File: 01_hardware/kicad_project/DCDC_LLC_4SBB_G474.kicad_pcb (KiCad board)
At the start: 4 copper layers, 160 x 105 mm, 237 parts, among them J1 VIN, J2 VOUT, J3 CAN, J4 CAN, J5 ADDR, J6 PROG, J7 SWD, Q1 NCEP0140AG, Q2 NCEP0160AG, Q3 NCEP0160AG, Q4 NCEP0140AG, Q5 NCEP0160AG, Q6 NCEP0160AG, Q7 BSC160N15NS5, Q8 BSC160N15NS5, SW1 DIP-6, T1 PQ2620, U1 STM32G474RBT6, U10 UCC27211DDAR, U11 UCC27524DR, U12 CA-IS3642LVW, U13 LMR16006XDDCR, U14 AMS1117-5.0, U15 LMV331IDBVR, U16 TL431AIDBZR, U2 UCC27211DDAR, U3 UCC27211DDAR, U4 LMR16006XDDCR, U5 AMS1117-5.0, U7 INA181A1IDBVR, U8 INA181A2IDBVR, U9 CA-IS3062VW, Y1 16MHz

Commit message: VIN monitor: sawtooth/comparator PWM over spare isolator channel to PA2 (TIM15_CH1)
- Primary: PNP current-source ramp (~5 ms) into 47 nF C0G, U17 reset detector,
  U18 PWM comparator vs OVP_DIV; R81/R82 now 0.1 %
- U12 VI2->VO2 carries VIN_PWM to PA2; R93 is its pull-down
- PCB: new block placed/routed below U15/U16, R106 moved for courtyard,
  GNDP island vias, silkscreen for new parts; DRC clean, netlist parity OK
- Outputs regenerated (BOM, Gerbers, CPL, EasyEDA, PDFs, pin-map)

Co-Authored-By: Claude Opus 5.5 <noreply@anthropic.com>
Claude-Session: https://claude.ai/code/session_01A35wrnwFKLPSaRSxxHs471
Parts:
- added C81: 1n, C_0402_1005Metric, F.Cu at (49.0, 96.0)
- added C82: 47n C0G 50V, C_0805_2012Metric, F.Cu at (47.4, 89.0)
- added C83: 100n, C_0402_1005Metric, F.Cu at (52.0, 86.4)
- added C84: 100n, C_0402_1005Metric, F.Cu at (60.0, 86.4)
- added D7: 1N4148W, D_SOD-123, F.Cu at (52.0, 93.6)
- added Q10: 2N7002, SOT-23, F.Cu at (46.6, 95.4)
- added Q9: MMBT3906, SOT-23, F.Cu at (43.4, 89.0)
- added R106: 1k, R_0402_1005Metric, F.Cu at (56.1, 92.0)
- added R107: 22k, R_0402_1005Metric, F.Cu at (50.4, 96.0)
- added R108: 10k, R_0402_1005Metric, F.Cu at (63.1, 88.6)
- added R109: 10k, R_0402_1005Metric, F.Cu at (56.9, 89.0)
- added R110: 1M, R_0402_1005Metric, F.Cu at (60.0, 91.6)
- added R86: 56k 1%, R_0402_1005Metric, F.Cu at (43.4, 85.8)
- added R87: 10k 1%, R_0402_1005Metric, F.Cu at (40.2, 87.6)
- added R88: 15k 1%, R_0402_1005Metric, F.Cu at (40.2, 90.6)
- added R89: 22R, R_0402_1005Metric, F.Cu at (46.6, 92.2)
- added U17: LMV331IDBVR, SOT-23-5, F.Cu at (52.0, 89.0)
- added U18: LMV331IDBVR, SOT-23-5, F.Cu at (60.0, 89.0)
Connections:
- R93 pad 1: SP_PA2 -> VIN_PWM
- U1 pad 14: SP_PA2 -> VIN_PWM
- U12 pad 13: (no net) -> VIN_PWM
- U12 pad 4: GNDP -> VINPWM_P
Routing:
- net VIN_PWM: track 0.00 -> 54.4 mm, vias 0 -> 4
- net +5V_P: track 68.5 -> 105.7 mm
- net VINPWM_P: track 0.00 -> 27.2 mm
- net RAMP_P: track 0.00 -> 17.7 mm, vias 0 -> 2
- net GATE_P: track 0.00 -> 13.9 mm
- net OVP_DIV: track 22.3 -> 33.7 mm, vias 2 -> 4
- net PB_P: track 0.00 -> 10.7 mm
- net VREF_P: track 10.1 -> 19.6 mm, vias 2 -> 4
- net RST_P: track 0.00 -> 8.25 mm
- net RAMPS_P: track 0.00 -> 7.21 mm
- net PE_P: track 0.00 -> 4.95 mm, vias 0 -> 2
- net SP_PA2: track 3.14 -> 0.00 mm
- net DIS_P: track 0.00 -> 2.85 mm
- net SR2_PWM: track 61.3 -> 58.8 mm
- net GNDP: track 105.4 -> 103.5 mm, vias 252 -> 245
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
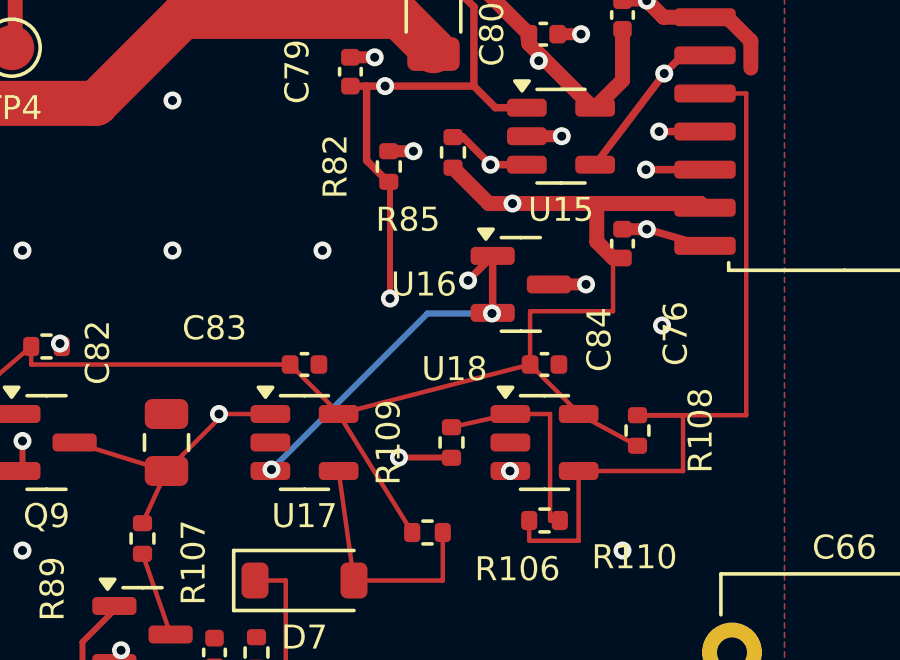
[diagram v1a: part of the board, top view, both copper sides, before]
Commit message: Review fixes: VIN monitor linearity and reset, full-scale summary, design notes
- U18 inputs swapped (IN+ = OVP_DIV, IN- = RAMP via R109 1k); R110 4.7M
  hysteresis now on the divider, not the ramp (old 1M path bent the ramp:
  +12.5 % error at 12 V; now < 0.02 % in simulation)
- Reset pulse hardened: C81 220p C0G, R107 100k so C82 always fully discharges
- OVP trip corrected to 50.26 V rising / 49.83 V falling; TL431A noted as 1 %
- PCB re-routed locally, values synced to schematic; DRC clean, parity OK,
  isolation 4.0 mm
- Design notes: full-scale and threshold summary, VIN monitor firmware formula
  and two-point calibration; exported to DOCX and PDF
- Pin-map, BOM, Gerbers, CPL, EasyEDA zip and PDFs regenerated

Co-Authored-By: Claude Opus 5.5 <noreply@anthropic.com>
Claude-Session: https://claude.ai/code/session_01A35wrnwFKLPSaRSxxHs471
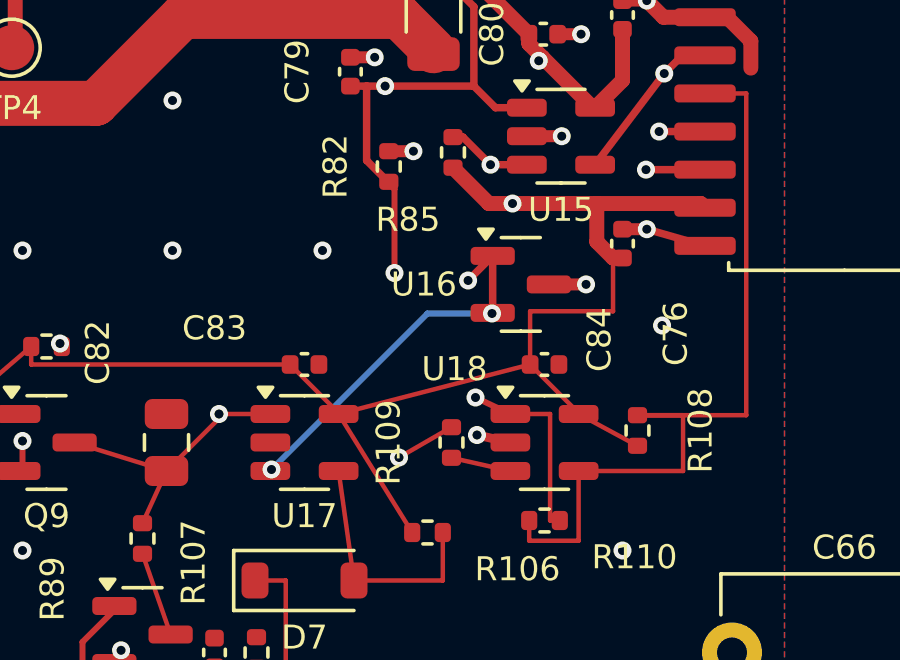
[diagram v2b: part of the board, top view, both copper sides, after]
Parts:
- C1, C11, C60: value 47u -> 47u 63V
- C56: value 2.2n -> 2.2n 2kV DNP
- C66: value 1n -> 1n Y1 DNP
- C81: value 1n -> 220p C0G
- CR1, CR2, CR3, CR4, CR5, CR6: value 100n -> 100n 100V C0G
- J1: value VIN -> VIN 12-48V
- J2: value VOUT -> VOUT 1.5-48V
- J3: value CAN -> CAN A
- J4: value CAN -> CAN B
- J5: value ADDR -> ADDR HDR
- J6: value PROG -> PROG PADS
- J7: value SWD -> ARM SWD 10
- L1: value 22u -> 22u 23A sat
- L2, L3: value 47u -> 47u 1A
- R107: value 22k -> 100k
- R109: value 10k -> 1k
- R110: value 1M -> 4.7M
- R81: value 191k 1% -> 191k 0.1%
- R82: value 10k 1% -> 10k 0.1%
- RS1: value 4m -> 4m 1% 2W
- RSH1: value 10m -> 10m 1% 1W
- T1: value PQ2620 -> PQ2620 4:8+8
- Y1: value 16MHz -> 16MHz 9pF
- turned R109 to -90 degrees
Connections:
- R110 pad 2: RAMPS_P -> OVP_DIV
- U18 pad 1: RAMPS_P -> OVP_DIV
- U18 pad 3: OVP_DIV -> RAMPS_P
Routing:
- net RAMPS_P: track 7.21 -> 2.01 mm
- net OVP_DIV: track 33.7 -> 37.2 mm
- net GNDP: track 103.5 -> 104.7 mm, vias 245 -> 246

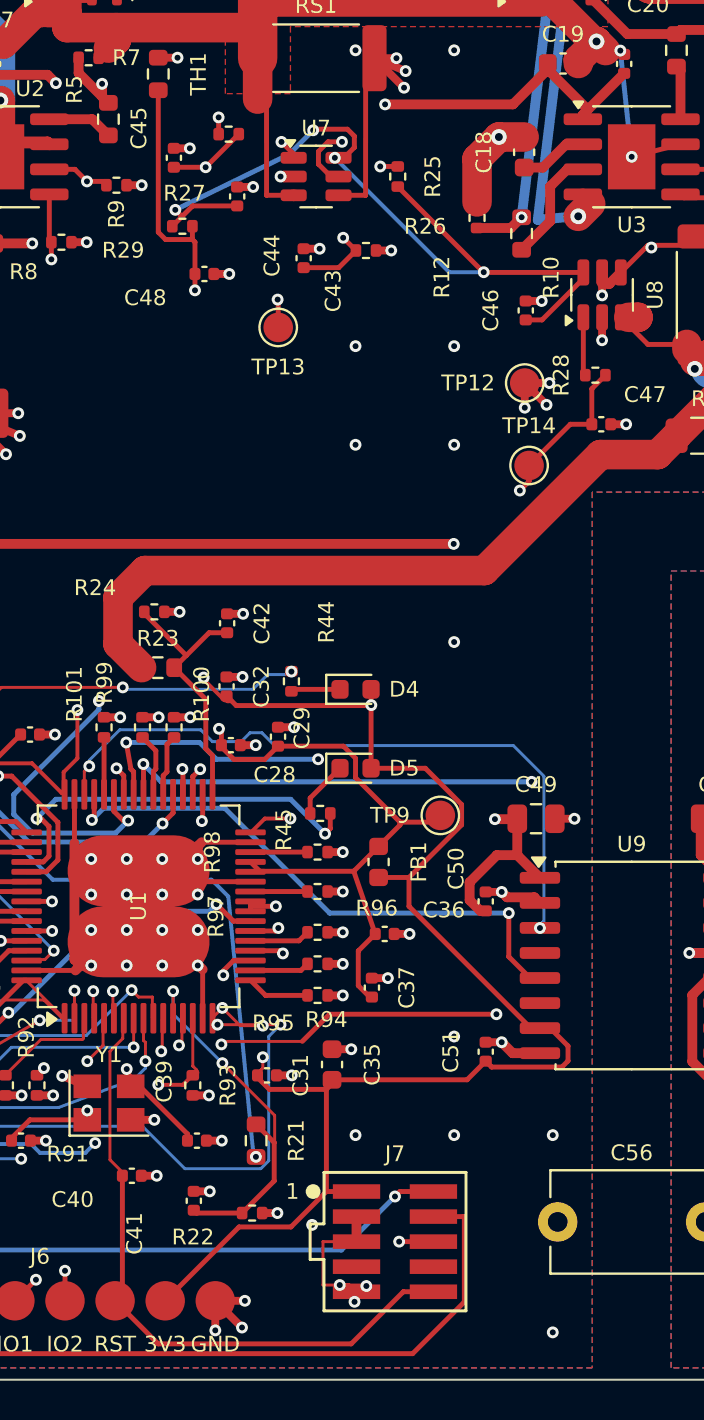
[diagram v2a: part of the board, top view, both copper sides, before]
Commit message: External REF3030 ADC reference; full review and documentation update
- U19 REF3030AIDBZR (3.000 V +/-0.2 %, LCSC C38423) + C85 drive VREF+ (new net
  VREF_ADC); VREF+ separated from VDDA; R25 (IL zero) and R29 (NTC pull-up)
  moved to VREF_ADC so those channels are ratiometric
- Full scales: VBUS/VOUT 61.8 V, IL +/-18.75 A, IOUT 6.0 A, DAC/COMP 0-3.0 V
- PCB: U19/C85 placed and routed, pins 28/29 hand-routed; DRC clean, parity
  OK, isolation 4.0 mm
- Design notes (DOCX/PDF), root and firmware READMEs, pin-map, layout review
  image, BOM, Gerbers, CPL, EasyEDA zip and PDFs updated

Co-Authored-By: Claude Opus 5.5 <noreply@anthropic.com>
Claude-Session: https://claude.ai/code/session_01A35wrnwFKLPSaRSxxHs471
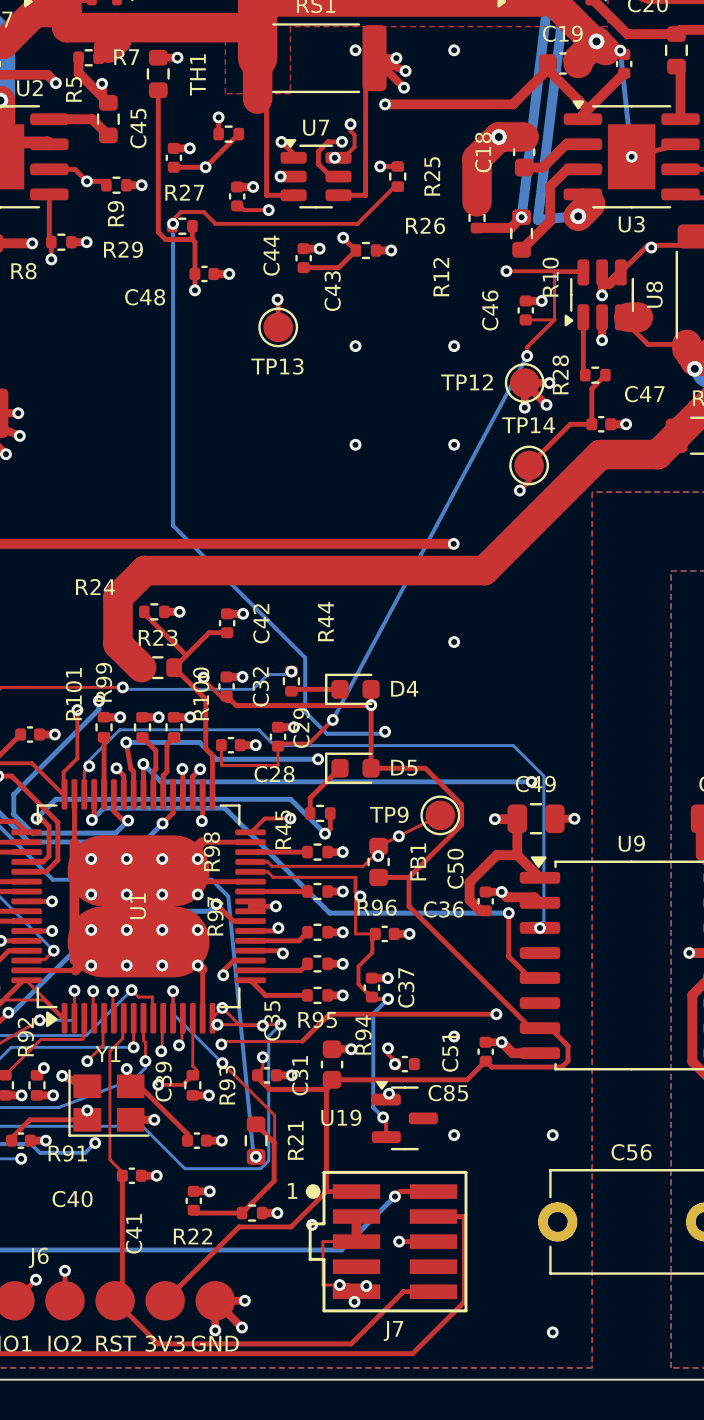
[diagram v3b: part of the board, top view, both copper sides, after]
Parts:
- added C85: 1u 10V, C_0402_1005Metric, F.Cu at (126.5, 89.0)
- added U19: REF3030AIDBZR, SOT-23, F.Cu at (126.5, 91.8)
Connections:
- C36 pad 1: +3V3A -> VREF_ADC
- C37 pad 1: +3V3A -> VREF_ADC
- R25 pad 1: +3V3A -> VREF_ADC
- R29 pad 1: +3V3A -> VREF_ADC
- U1 pad 28: +3V3A -> VREF_ADC
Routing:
- net VREF_ADC: track 0.00 -> 76.6 mm, vias 0 -> 5
- net +3V3A: track 100.2 -> 95.0 mm, vias 5 -> 11
- net NTC_SNS: track 49.6 -> 48.8 mm
- net GND: vias 286 -> 285

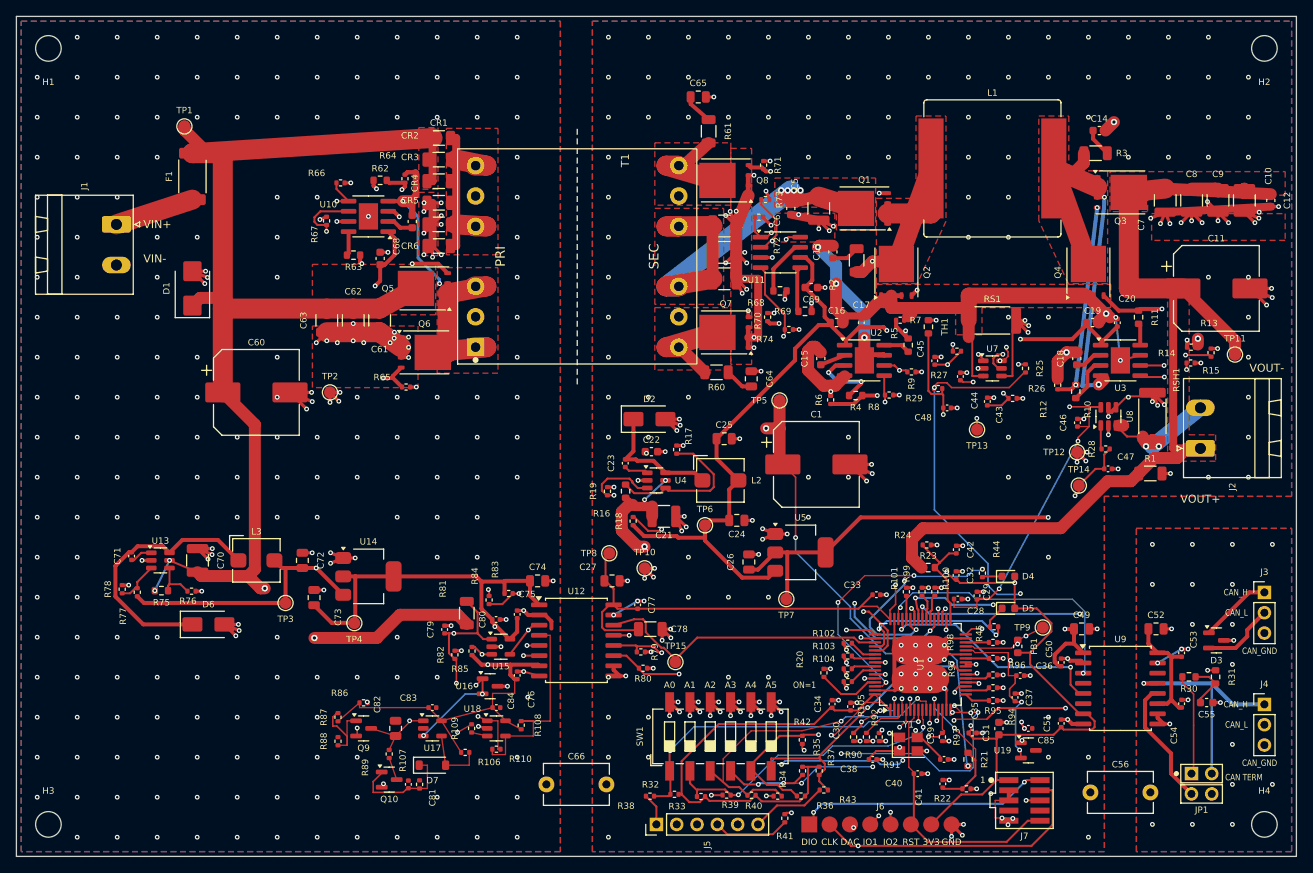
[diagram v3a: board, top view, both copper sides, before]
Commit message: Comply with JLCPCB 4-layer capabilities (2 oz outer)
- PTH pad to track >= 0.28 mm: J5 ADDR_H3 (F.Cu) and ADDR_H2 (In2) re-routed,
  J3/J4 CAN In2 runs 0.4 mm, unused inner annular rings removed on J3/J4/J5
- Silkscreen: all text >= 1.0 mm high, 0.15 mm stroke; only 2 references moved
- New kicad_dru with the JLC limits as custom DRC rules; DRC 0 errors / 0
  warnings with them loaded, parity OK, isolation 4.0 mm
- Gerbers, CPL, PCB PDF, EasyEDA zip, design notes and README updated

Co-Authored-By: Claude Opus 5.5 <noreply@anthropic.com>
Claude-Session: https://claude.ai/code/session_01A35wrnwFKLPSaRSxxHs471
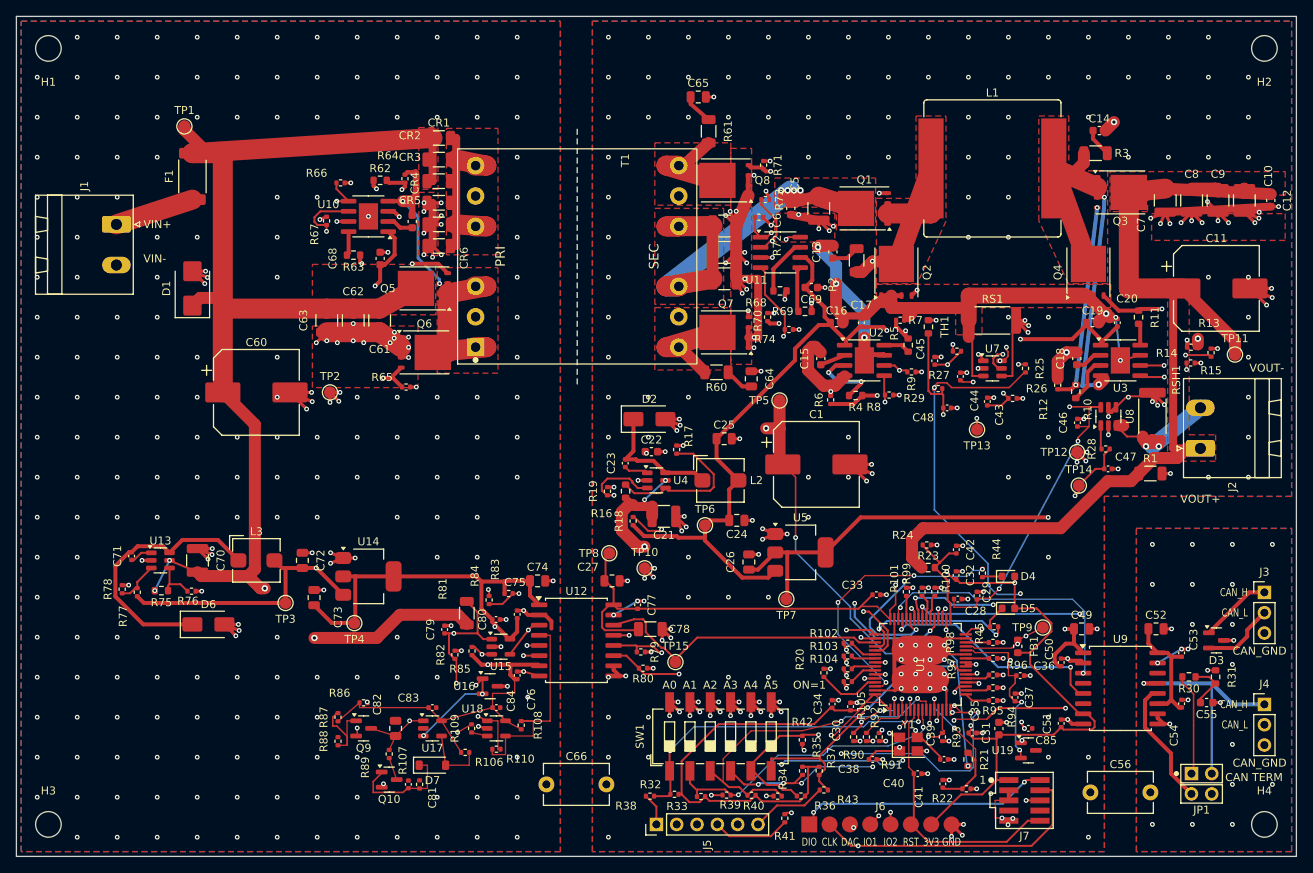
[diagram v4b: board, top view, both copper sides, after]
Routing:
- net ADDR_H2: track 13.0 -> 13.8 mm
